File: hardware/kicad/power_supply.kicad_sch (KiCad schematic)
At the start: 0 parts

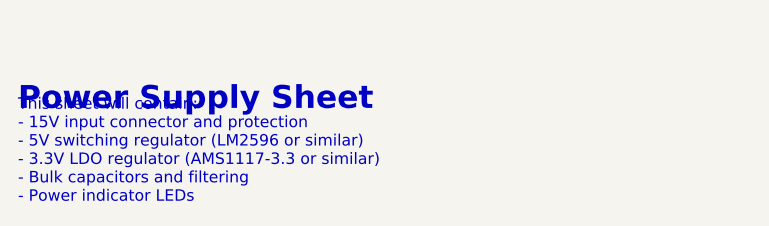
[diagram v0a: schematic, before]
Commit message: Add CLI, persistent config, AC frequency monitor, and pulse outputs
Features:
- USB CLI with commands: help, status, pins, acfreq, debug, config, wifi, pulse, reboot
- Persistent flash configuration with CRC32 validation (config save/show/reset)
- WiFi auto-connect on boot using saved credentials
- AC mains frequency monitor via zero-crossing detector (GP19)
- Configurable pulse outputs with interval/second/minute/time modes
- Debug on/off command to control periodic status output

Fixes:
- Watchdog timeout during 30s WiFi connect (extend to 35s during connect)
- Flash write safety with PICO_FLASH_ASSUME_CORE1_SAFE for CYW43 compatibility

Build:
- Added make flash target with automatic bootloader reboot
- Added pico_flash and pico_multicore libraries

Documentation:
- Updated Phase-03 with AC-to-DC conversion chain and zero-crossing circuit
- Updated Hardware Guide docx with power supply block diagram image
- Regenerated power_supply.png with complete AC-to-DC diagram

🤖 Generated with [Claude Code](https://claude.com/claude-code)

Co-Authored-By: Claude Opus 4.5 <noreply@anthropic.com>
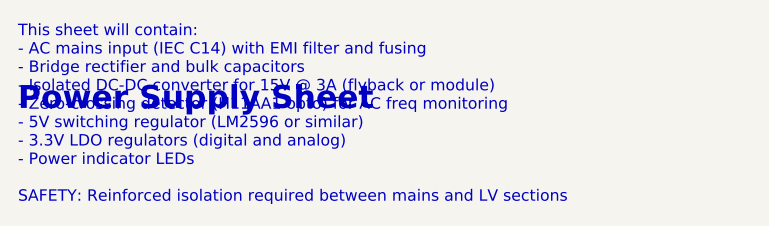
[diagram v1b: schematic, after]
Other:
- note added: "This sheet will contain: - AC mains input (IEC C14) with EMI filter and fusing - Bridge rectifier and bulk capacitors - Isolated DC-DC converter for 15V @ 3A (flyback or module) - Zero-crossing detector (H11AA1 opto) for AC freq monitoring - 5V switching regulator (LM2596 or similar) - 3.3V LDO regulators (digital and analog) - Power indicator LEDs SAFETY: Reinforced isolation required between ma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"
- note removed: "This sheet will contain: - 15V input connector and protection - 5V switching regulator (LM2596 or similar) - 3.3V LDO regulator (AMS1117-3.3 or similar) - Bulk capacitors and filtering - Power indicator LEDs"
- title: Power Supply - 15V/5V/3.3V Rails -> Power Supply - AC Mains Input with Frequency Monitor
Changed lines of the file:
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@@
 	(paper "A4")
 	(title_block
-		(title "Power Supply - 15V/5V/3.3V Rails")
-		(date "2024-12-20")
-		(rev "1.0")
+		(title "Power Supply - AC Mains Input with Frequency Monitor")
+		(date "2024-12-21")
+		(rev "2.0")
 		(company "CHRONOS-Rb Project")
-		(comment 1 "Input: 15V DC for FE-5680A")
-		(comment 2 "Outputs: +15V, +5V, +3.3V regulated rails")
-		(comment 3 "Power budget: ~15W peak during warmup")
+		(comment 1 "Input: 100-240V AC 50/60Hz Universal Mains")
+		(comment 2 "Outputs: +15V/3A, +5V/1A, +3.3V regulated rails")
+		(comment 3 "Features: Isolated AC-DC, Zero-crossing freq monitor")
+		(comment 4 "WARNING: Contains hazardous mains voltage")
 	)
 	(text "Power Supply Sheet"
@@
 		)
 	)
-	(text "This sheet will contain:\n- 15V input connector and protection\n- 5V switching regulator (LM2596 or similar)\n- 3.3V LDO regulator (AMS1117-3.3 or similar)\n- Bulk capacitors and filtering\n- Power indicator LEDs"
+	(text "This sheet will contain:\n- AC mains input (IEC C14) with EMI filter and fusing\n- Bridge rectifier and bulk capacitors\n- Isolated DC-DC converter for 15V @ 3A (flyback or module)\n- Zero-crossing detector (H11AA1 opto) for AC freq monitoring\n- 5V switching regulator (LM2596 or similar)\n- 3.3V LDO regulators (digital and analog)\n- Power indicator LEDs\n\nSAFETY: Reinforced isolation required between mains and LV sections"
 		(exclude_from_sim no)
 		(at 50.8 60.96 0)
